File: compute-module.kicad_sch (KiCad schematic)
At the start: 85 parts, among them J1 DF40HC(3.0)-100DS-0.4v, J2 DF40HC(3.0)-100DS-0.4v, M1 compute-module-4-1.5mm

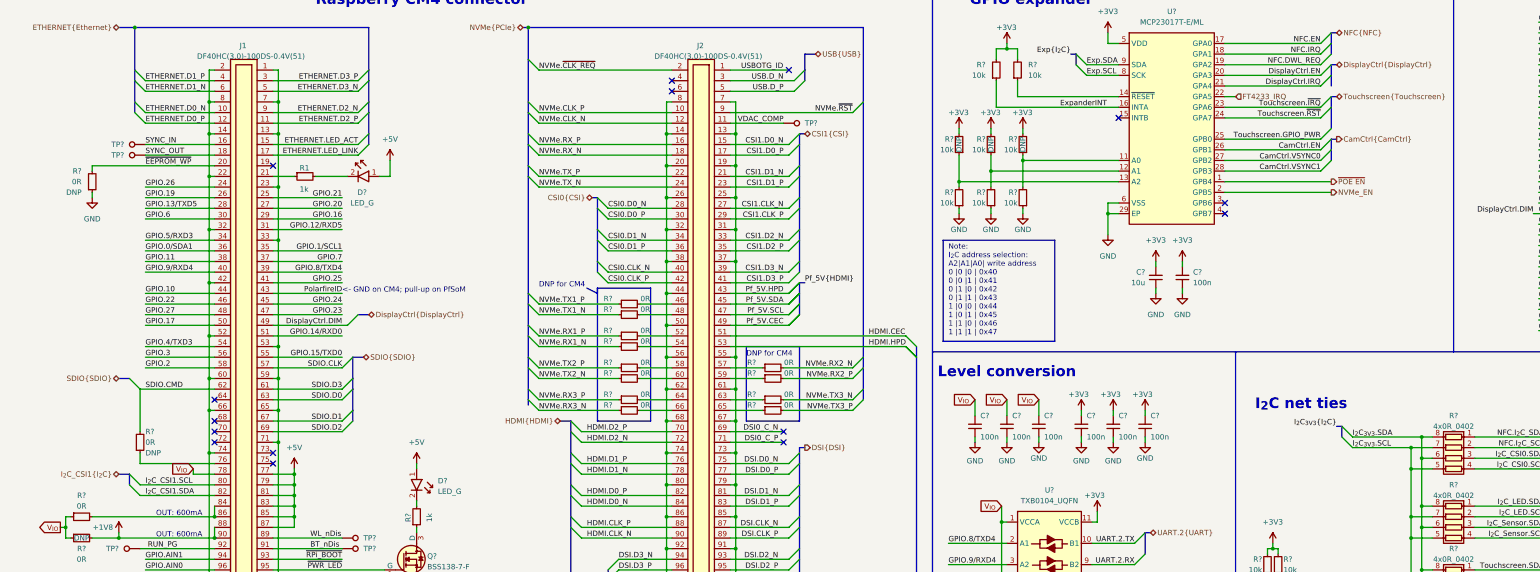
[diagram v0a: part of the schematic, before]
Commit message: [#54617] Apply changes pointed in review, related to nvme-micro-sd
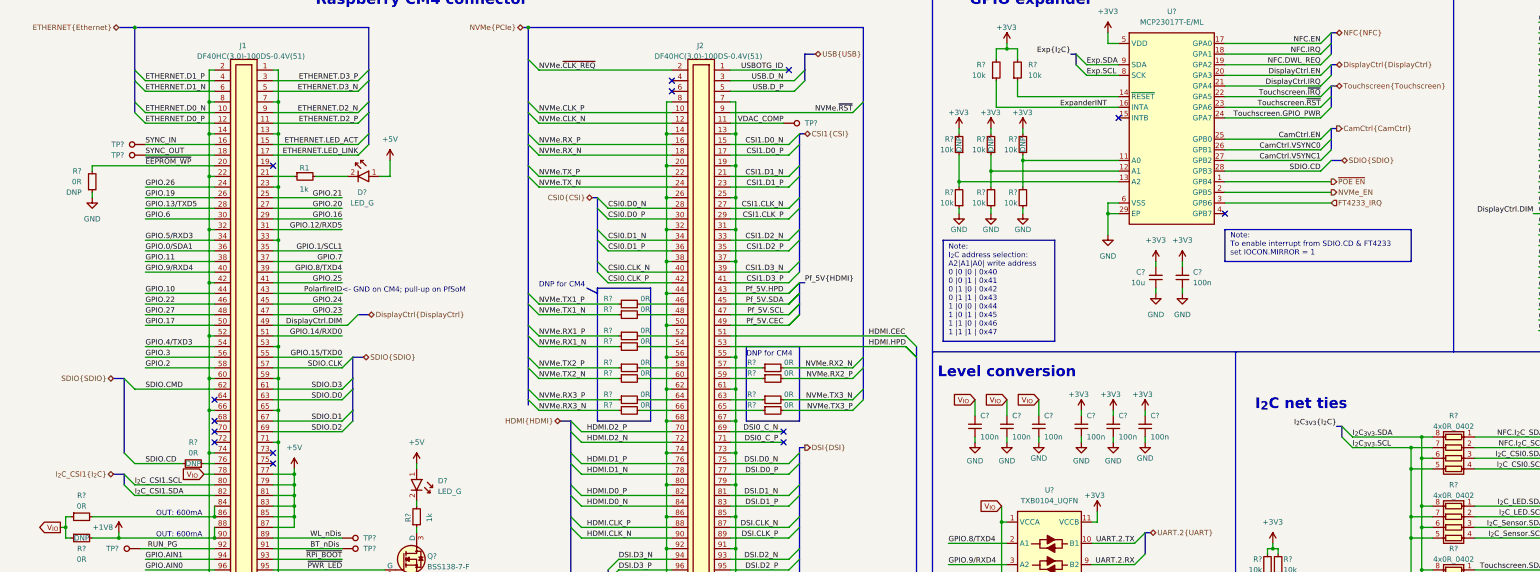
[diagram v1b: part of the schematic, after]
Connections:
- net CamCtrl.EN: now also U?.25 (GPB0); no longer U?.26 (GPB1)
- net CamCtrl.VSYNC0: now also U?.26 (GPB1); no longer U?.27 (GPB2)
- net CamCtrl.VSYNC1: now also U?.27 (GPB2); no longer U?.28 (GPB3)
- net FT4233_IRQ: now also U?.3 (GPB6); no longer U?.22 (GPA5)
- net SDIO.CMD: no longer R?.2
- net Touchscreen.GPIO_PWR: now also U?.24 (GPA7); no longer U?.25 (GPB0)
- net Touchscreen.~{IRQ}: now also U?.22 (GPA5); no longer U?.23 (GPA6)
- net Touchscreen.~{RST}: now also U?.23 (GPA6); no longer U?.24 (GPA7)
- new net SDIO.CD: R?.2, U?.28 (GPB3)
- no-connect marks 15 -> 14
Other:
- note added: "Note: To enable interrupt from SDIO.CD & FT4233 set IOCON.MIRROR = 1"
- moved on the sheet: R?

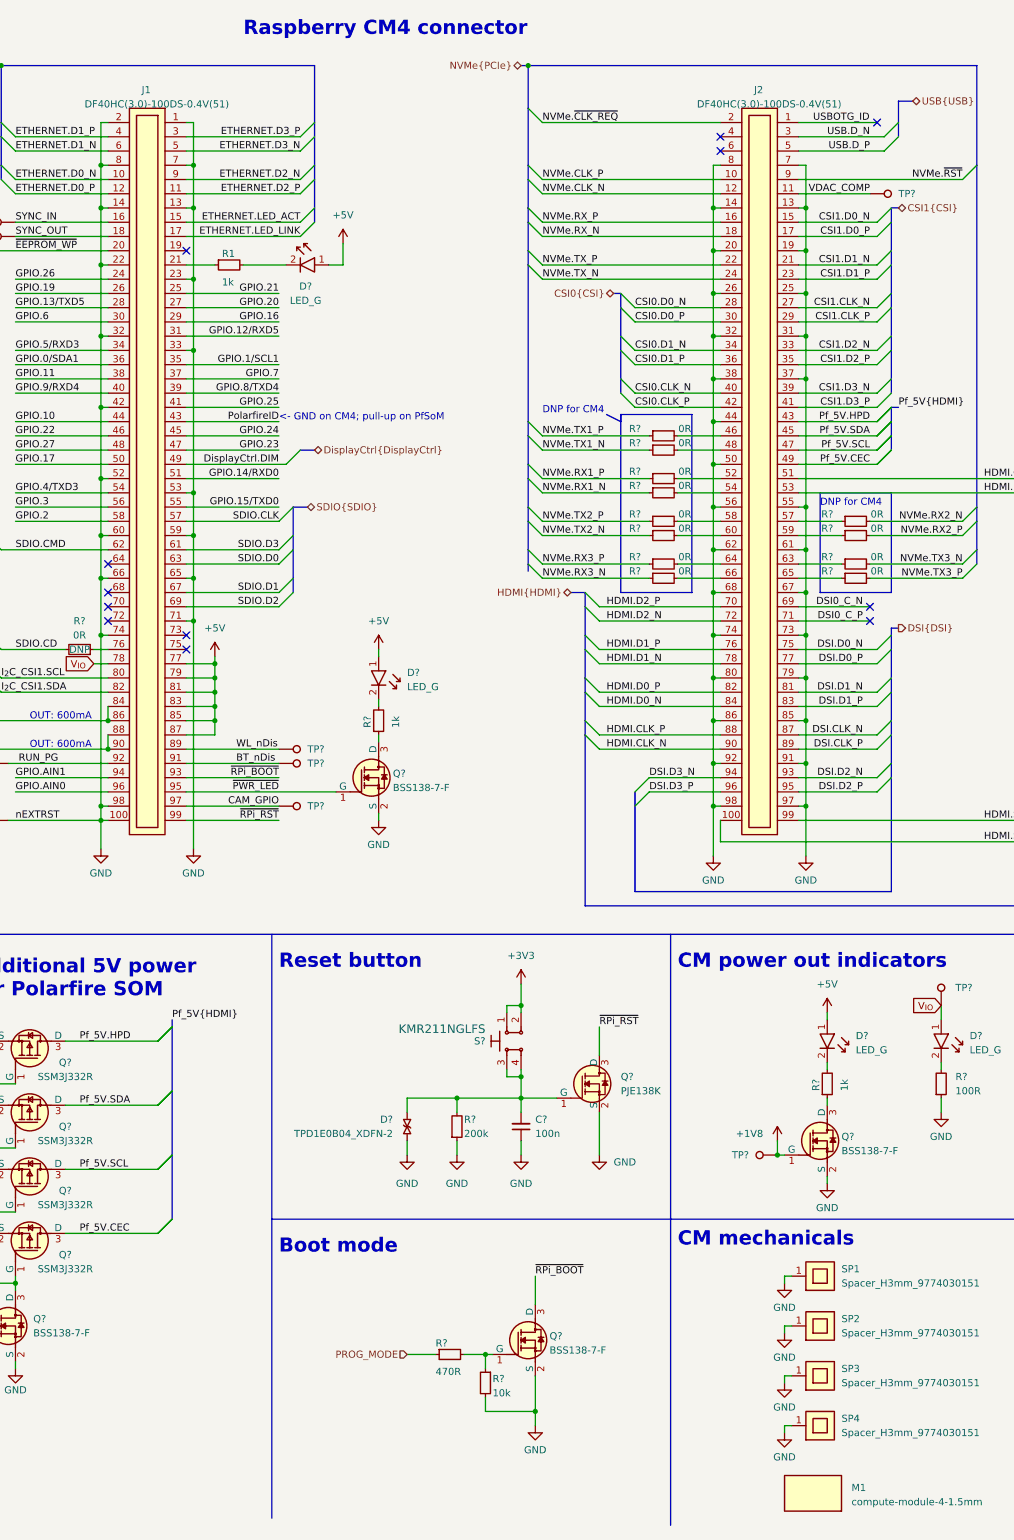
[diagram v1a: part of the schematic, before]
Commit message: [#54617] Add wakeup button to CM; Add some testpoints to CM
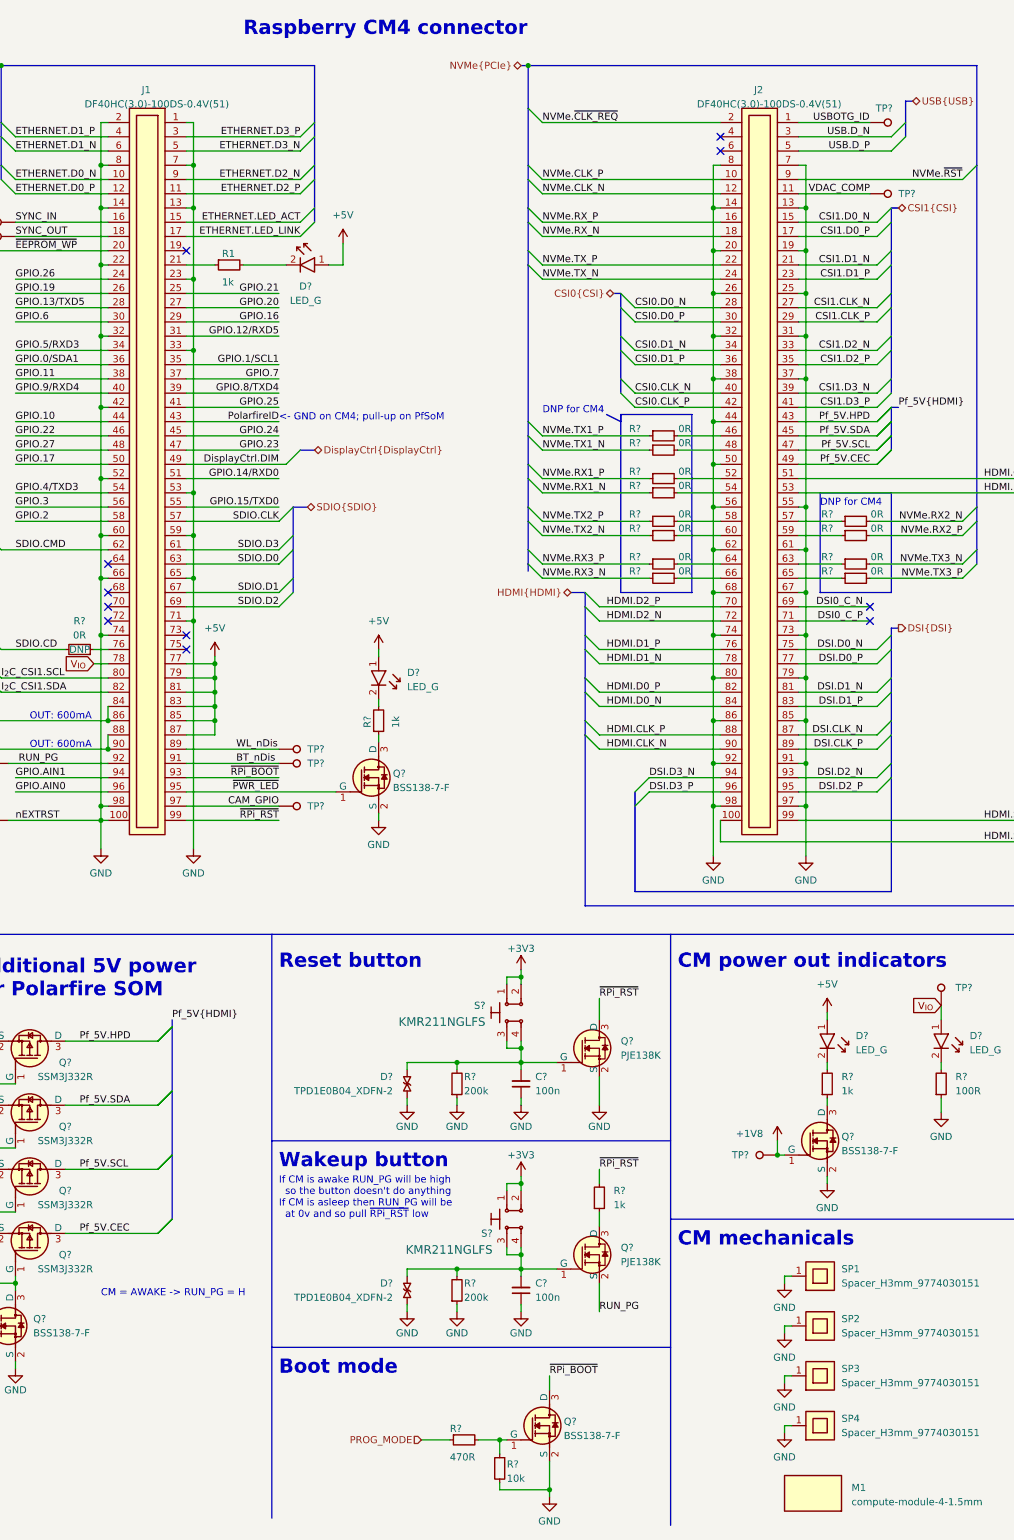
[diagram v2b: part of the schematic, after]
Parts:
- added C?: C_100n_0402, antmicro-footprints:C_0402_1005Metric, symbol antmicroCapacitors0402:C_100n_0402
- added D?: TPD1E0B04_XDFN-2, antmicro-footprints:XDFN-2_1x0.60mm, symbol antmicroTVSDiodes:TPD1E0B04_XDFN-2
- added Q?: PJE138K, antmicro-footprints:SOT-523, symbol antmicroTransistorsFETsMOSFETsSingle:PJE138K
- added R?: R_1k_0603, antmicro-footprints:R_0603_1608Metric, symbol antmicroResistors0603:R_1k_0603
- added R?: R_200k_0402, antmicro-footprints:R_0402_1005Metric, symbol antmicroResistors0402:R_200k_0402
- added S?: SW_KMR211NGLFS_SMD, antmicro-footprints:SW_KMR211NGLFS_SMD, symbol antmicroPushbuttonSwitches:SW_KMR211NGLFS_SMD
- added TP?: TP_1mm_SMD, antmicro-footprints:TP_SMD_1mm, symbol antmicroTestPoints:TP_1mm_SMD
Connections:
- net +3V3: now also S?.1, S?.2
- net GND: now also C?.1, D?.1, R?.1
- net RUN_PG: now also Q?.2 (S)
- net USBOTG_ID: now also TP?.1
- net ~{RPi_RST}: now also R?.2
- new net: C?.2, D?.2, Q?.1 (G), R?.2, S?.3, S?.4
- new net: Q?.3 (D), R?.1
- no-connect marks 14 -> 13
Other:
- note added: "CM = AWAKE -> RUN_PG = H"
- note added: "If CM is awake RUN_PG will be high so the button doesn't do anything If CM is asleep then RUN_PG will be at 0v and so pull ~{RPi_RST} low"
- note added: "Wakeup button"
- moved on the sheet: C?, D?, Q?, R?, S?

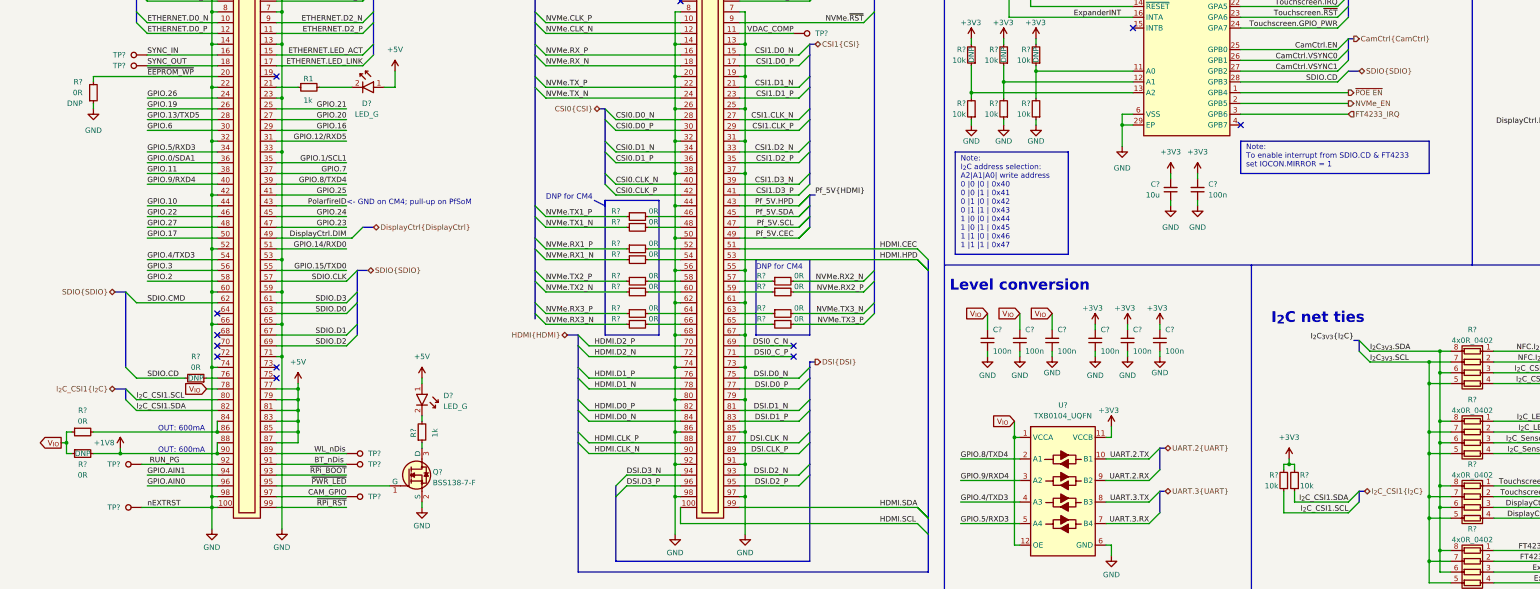
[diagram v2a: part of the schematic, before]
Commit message: [#54617] Change how CSI switches decoupling capacitors are placed on schematic
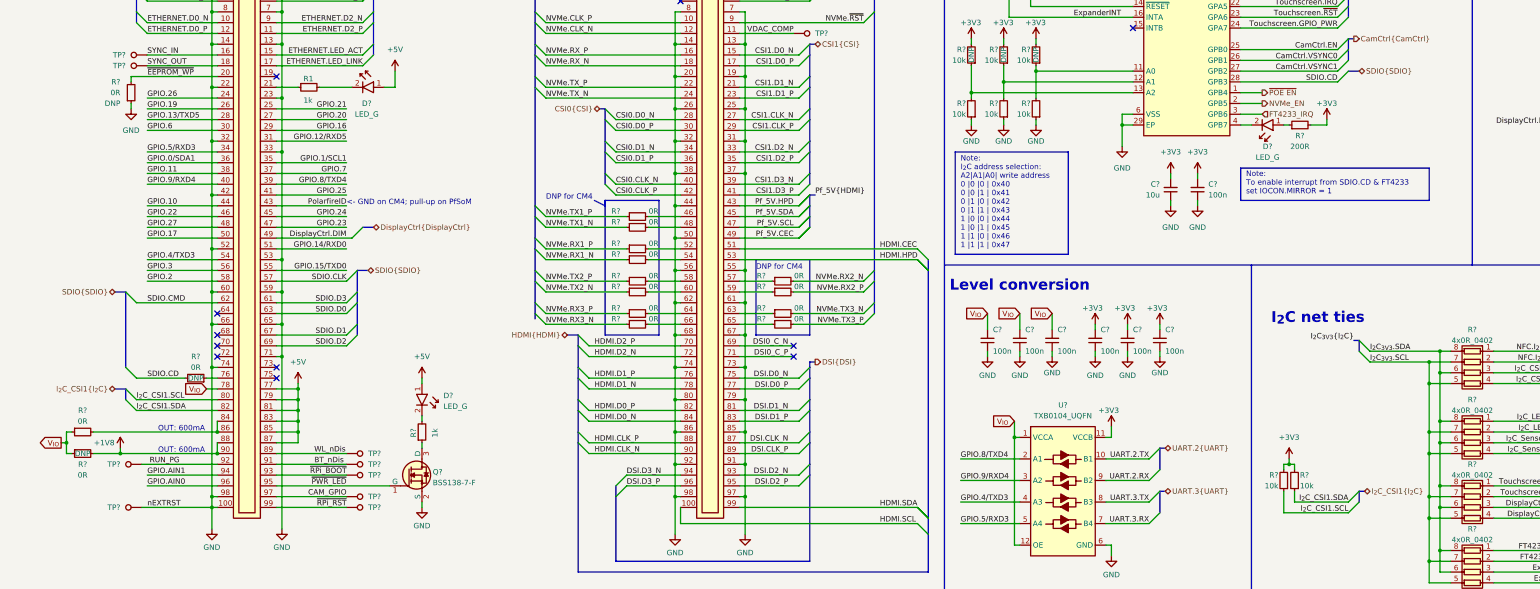
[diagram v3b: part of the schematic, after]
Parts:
- added D?: LED_G, antmicro-footprints:LED_0603_1608Metric_R, symbol antmicroLEDIndicationDiscrete:LED_R_0603_598-8D80-107F
- added R?: R_200R_0402, antmicro-footprints:R_0402_1005Metric, symbol antmicroResistors0402:R_200R_0402
- added TP? (x2): TP_1mm_SMD, antmicro-footprints:TP_SMD_1mm, symbol antmicroTestPoints:TP_1mm_SMD
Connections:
- net +3V3: now also R?.2
- net ~{RPi_BOOT}: now also TP?.1
- net ~{RPi_RST}: now also TP?.1
- net at U?.4 (GPB7): now also D?.2
- new net: D?.1, R?.1
- no-connect marks 13 -> 12
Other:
- moved on the sheet: R?
